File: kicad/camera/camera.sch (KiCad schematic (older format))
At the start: 0 parts

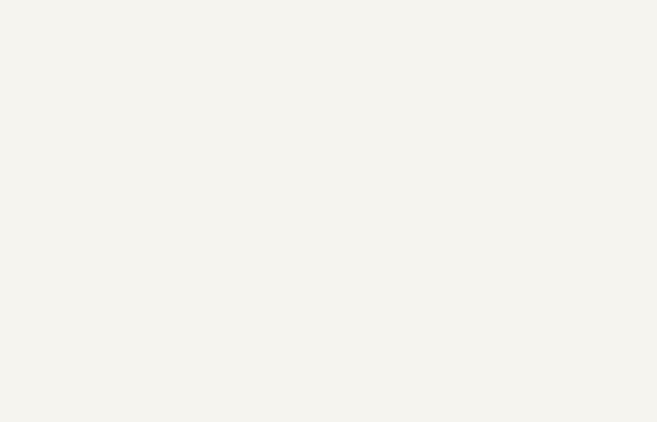
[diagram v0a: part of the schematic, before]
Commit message: Adding Spartan_ESP scheme
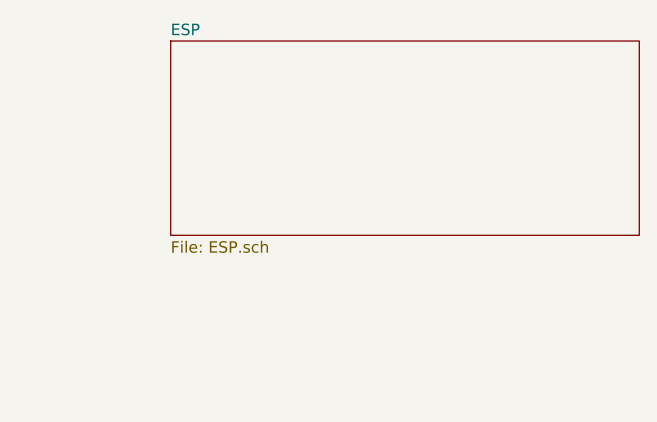
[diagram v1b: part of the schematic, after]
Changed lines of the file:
@@
 $Descr A4 11693 8268
 encoding utf-8
-Sheet 1 4
+Sheet 1 5
 Title ""
 Date ""
@@
 F1 "flash.sch" 50
 $EndSheet
+$Sheet
+S 7100 1600 2050 850
+U 5FE78D9F
+F0 "ESP" 50
+F1 "ESP.sch" 50
+$EndSheet
 $EndSCHEMATC
